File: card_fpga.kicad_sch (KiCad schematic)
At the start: 2 parts, among them U1 LFE5U-25F-6BG381C, Y1 FNETHE025

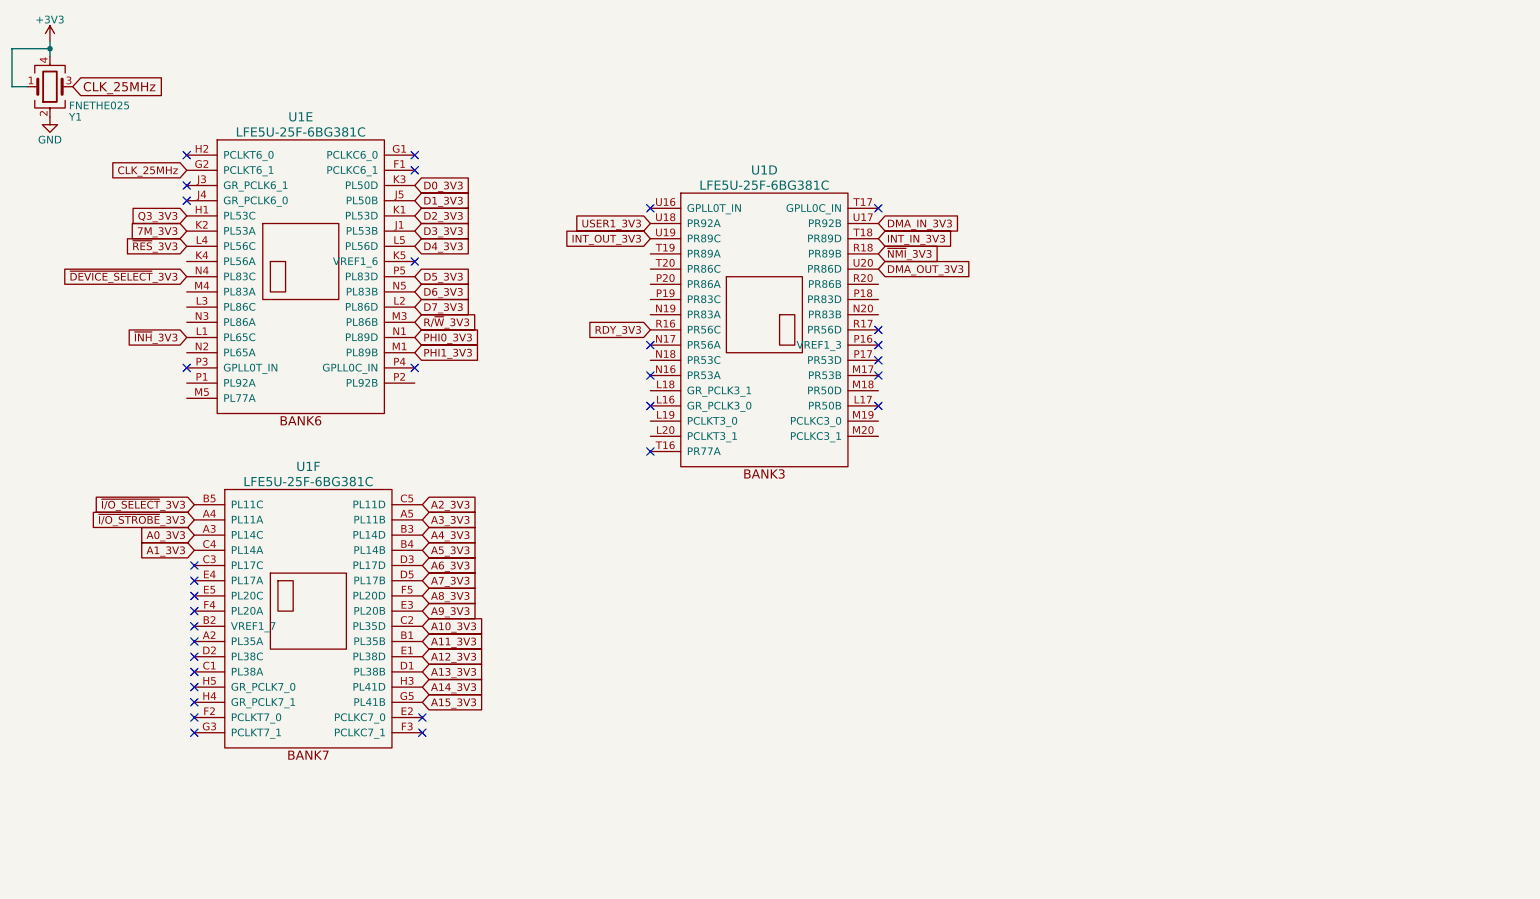
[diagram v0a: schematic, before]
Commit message: Moved routing to right side of FPGA
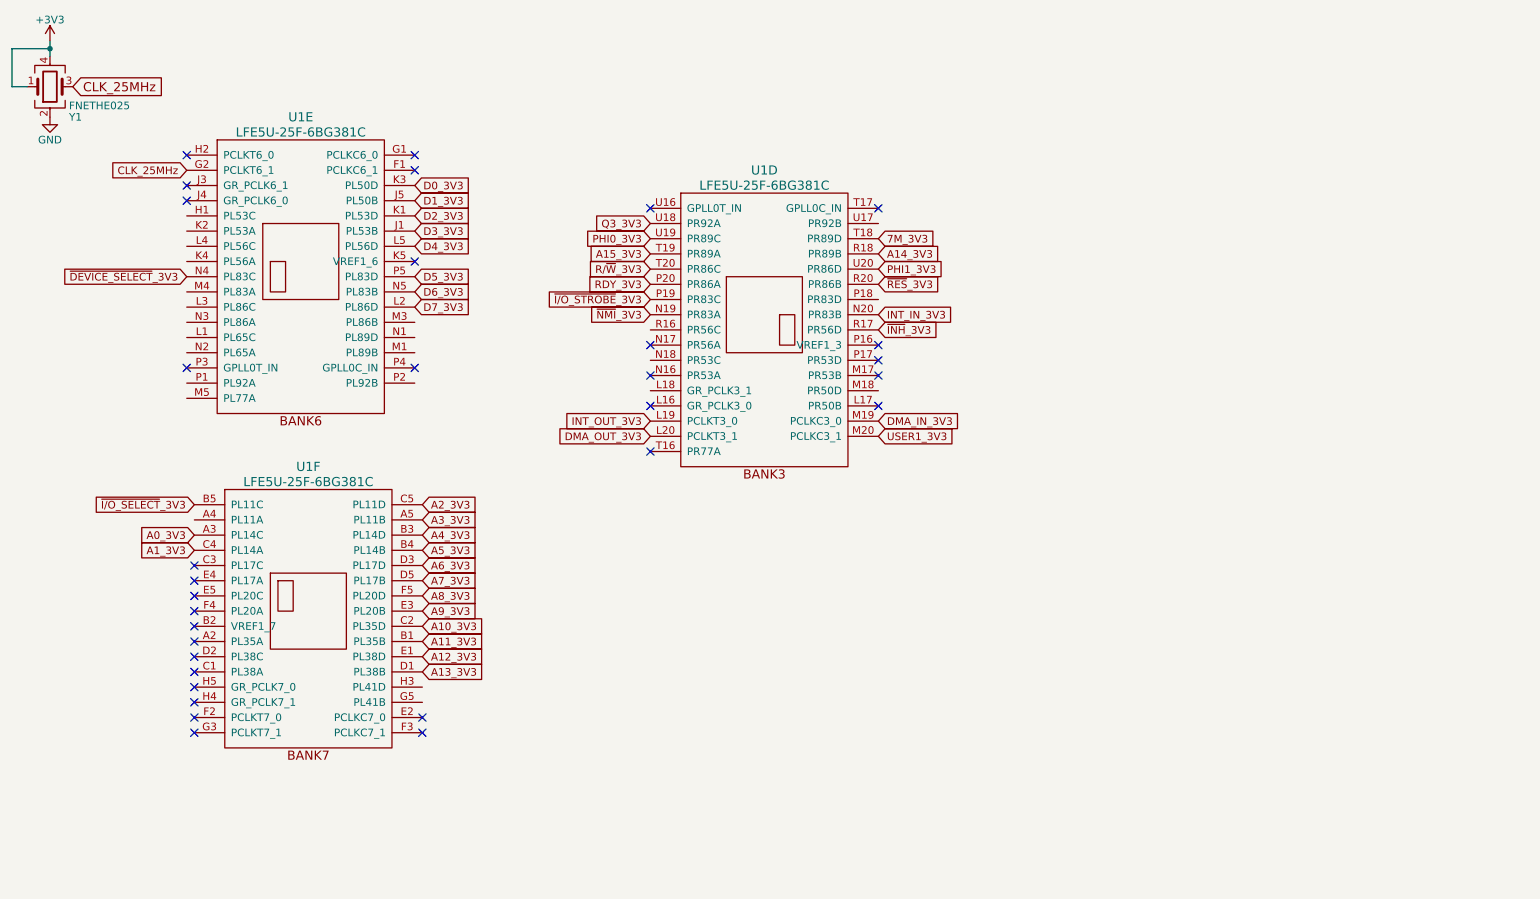
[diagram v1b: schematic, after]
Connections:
- net 7M_3V3: now also U1.T18 (PR89D); no longer U1.K2 (PL53A)
- net A14_3V3: now also U1.R18 (PR89B); no longer U1.H3 (PL41D)
- net A15_3V3: now also U1.T19 (PR89A); no longer U1.G5 (PL41B)
- net DMA_IN_3V3: now also U1.M19 (PCLKC3_0); no longer U1.U17 (PR92B)
- net DMA_OUT_3V3: now also U1.L20 (PCLKT3_1); no longer U1.U20 (PR86D)
- net INT_IN_3V3: now also U1.N20 (PR83B); no longer U1.T18 (PR89D)
- net INT_OUT_3V3: now also U1.L19 (PCLKT3_0); no longer U1.U19 (PR89C)
- net PHI0_3V3: now also U1.U19 (PR89C); no longer U1.N1 (PL89D)
- net PHI1_3V3: now also U1.U20 (PR86D); no longer U1.M1 (PL89B)
- net Q3_3V3: now also U1.U18 (PR92A); no longer U1.H1 (PL53C)
- net RDY_3V3: now also U1.P20 (PR86A); no longer U1.R16 (PR56C)
- net R/~{W}_3V3: now also U1.T20 (PR86C); no longer U1.M3 (PL86B)
- net USER1_3V3: now also U1.M20 (PCLKC3_1); no longer U1.U18 (PR92A)
- net ~{INH}_3V3: now also U1.R17 (PR56D); no longer U1.L1 (PL65C)
- net ~{I/O_STROBE}_3V3: now also U1.P19 (PR83C); no longer U1.A4 (PL11A)
- net ~{NMI}_3V3: now also U1.N19 (PR83A); no longer U1.R18 (PR89B)
- net ~{RES}_3V3: now also U1.R20 (PR86B); no longer U1.L4 (PL56C)
- no-connect marks 33 -> 32

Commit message: Routed Level Shifters + Flash
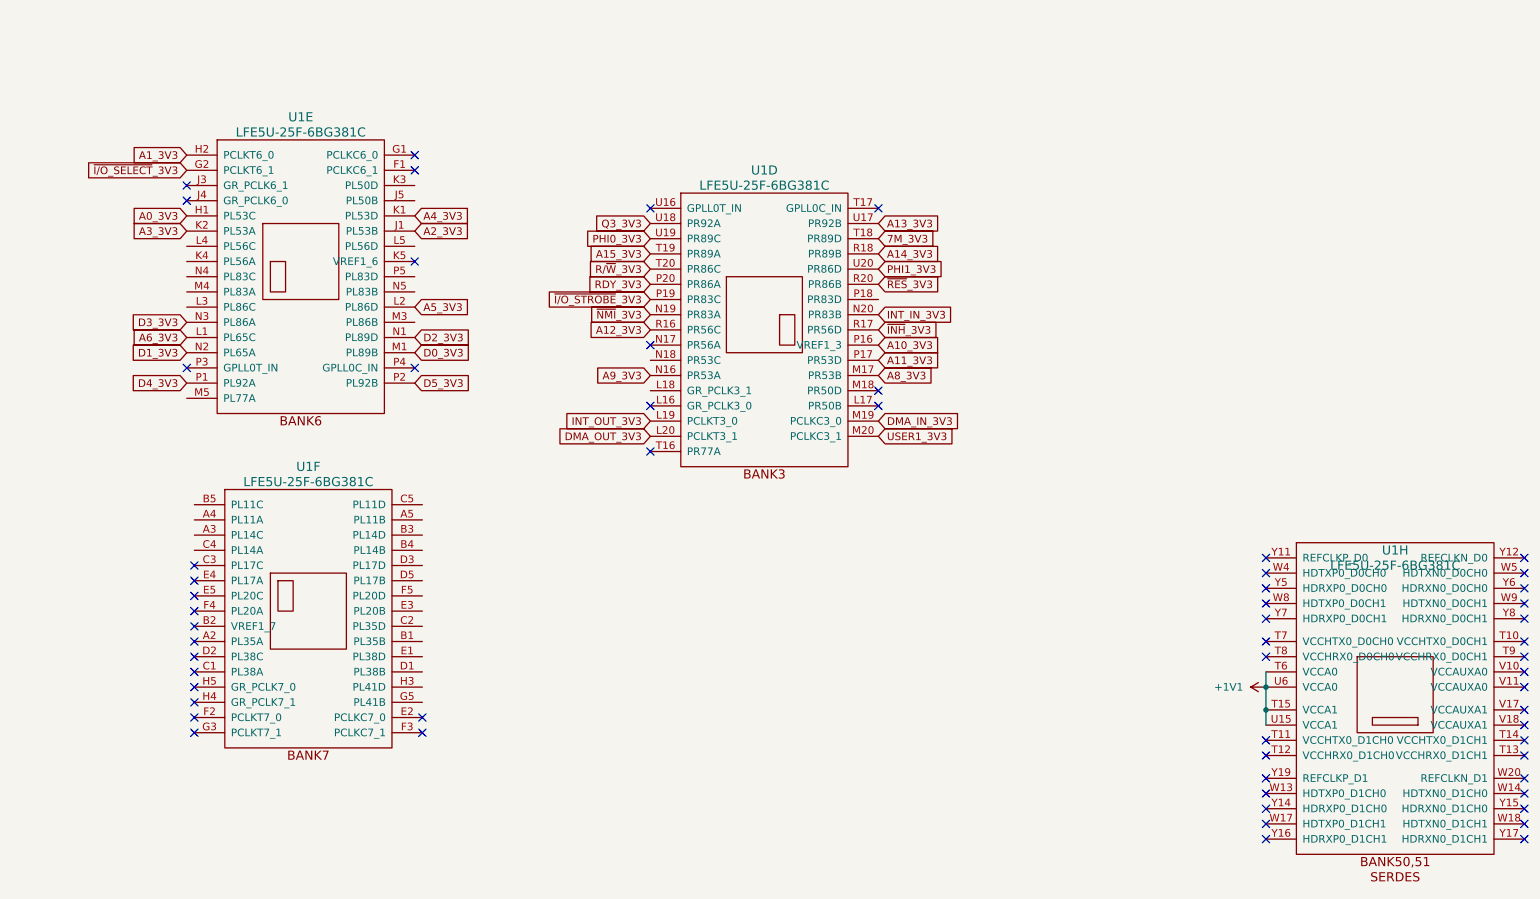
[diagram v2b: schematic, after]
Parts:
- removed Y1: FNETHE025, oscxo:Crystal_SMD_7050_4Pads, symbol Device:Crystal_GND24
- added unit 8 of U1
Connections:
- net CLK_25MHz is gone; now on net ~{I/O_SELECT}_3V3: U1.G2 (PCLKT6_1)
- net D7_3V3 is gone; now on net A5_3V3: U1.L2 (PL86D)
- net A0_3V3: now also U1.H1 (PL53C); no longer U1.A3 (PL14C)
- net A10_3V3: now also U1.P16 (VREF1_3); no longer U1.C2 (PL35D)
- net A11_3V3: now also U1.P17 (PR53D); no longer U1.B1 (PL35B)
- net A12_3V3: now also U1.R16 (PR56C); no longer U1.E1 (PL38D)
- net A13_3V3: now also U1.U17 (PR92B); no longer U1.D1 (PL38B)
- net A1_3V3: now also U1.H2 (PCLKT6_0); no longer U1.C4 (PL14A)
- net A2_3V3: now also U1.J1 (PL53B); no longer U1.C5 (PL11D)
- net A3_3V3: now also U1.K2 (PL53A); no longer U1.A5 (PL11B)
- net A4_3V3: now also U1.K1 (PL53D); no longer U1.B3 (PL14D)
- net A5_3V3: no longer U1.B4 (PL14B)
- net A6_3V3: now also U1.L1 (PL65C); no longer U1.D3 (PL17D)
- net A8_3V3: now also U1.M17 (PR53B); no longer U1.F5 (PL20D)
- net A9_3V3: now also U1.N16 (PR53A); no longer U1.E3 (PL20B)
- net D0_3V3: now also U1.M1 (PL89B); no longer U1.K3 (PL50D)
- net D1_3V3: now also U1.N2 (PL65A); no longer U1.J5 (PL50B)
- net D2_3V3: now also U1.N1 (PL89D); no longer U1.K1 (PL53D)
- net D3_3V3: now also U1.N3 (PL86A); no longer U1.J1 (PL53B)
- net D4_3V3: now also U1.P1 (PL92A); no longer U1.L5 (PL56D)
- net D5_3V3: now also U1.P2 (PL92B); no longer U1.P5 (PL83D)
- net ~{I/O_SELECT}_3V3: no longer U1.B5 (PL11C)
- net A7_3V3: no longer names the net of U1.D5 (PL17B)
- net D6_3V3: no longer names the net of U1.N5 (PL83B)
- net ~{DEVICE_SELECT}_3V3: no longer names the net of U1.N4 (PL83C)
- new net +1V1: U1.T15 (VCCA1), U1.T6 (VCCA0), U1.U15 (VCCA1), U1.U6 (VCCA0)
- no-connect marks 32 -> 60

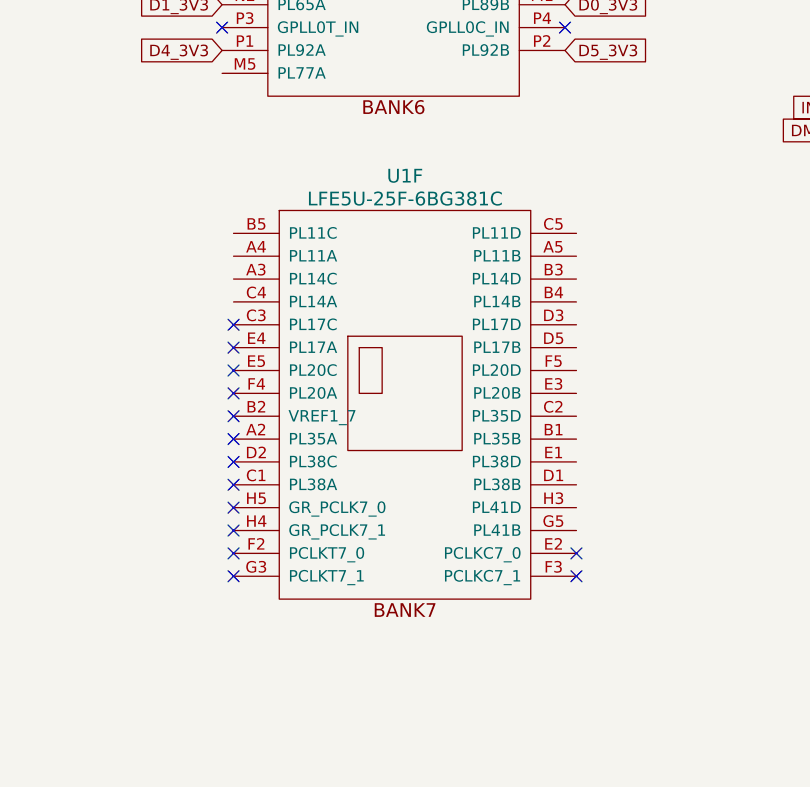
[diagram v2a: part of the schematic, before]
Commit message: Started SRAM routing
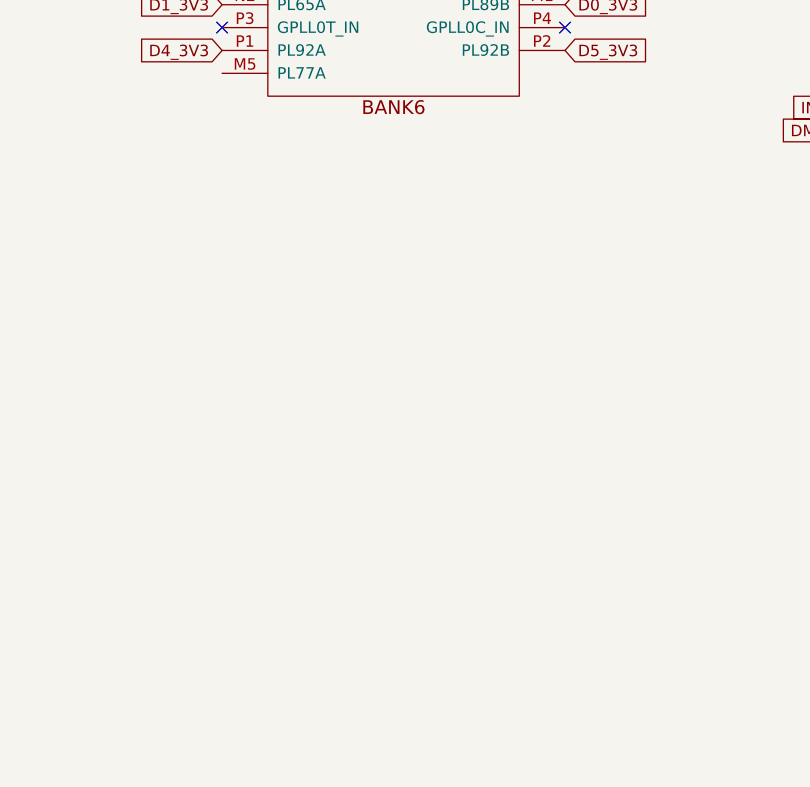
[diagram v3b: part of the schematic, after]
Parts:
- removed unit 6 of U1
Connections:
- no-connect marks 60 -> 46

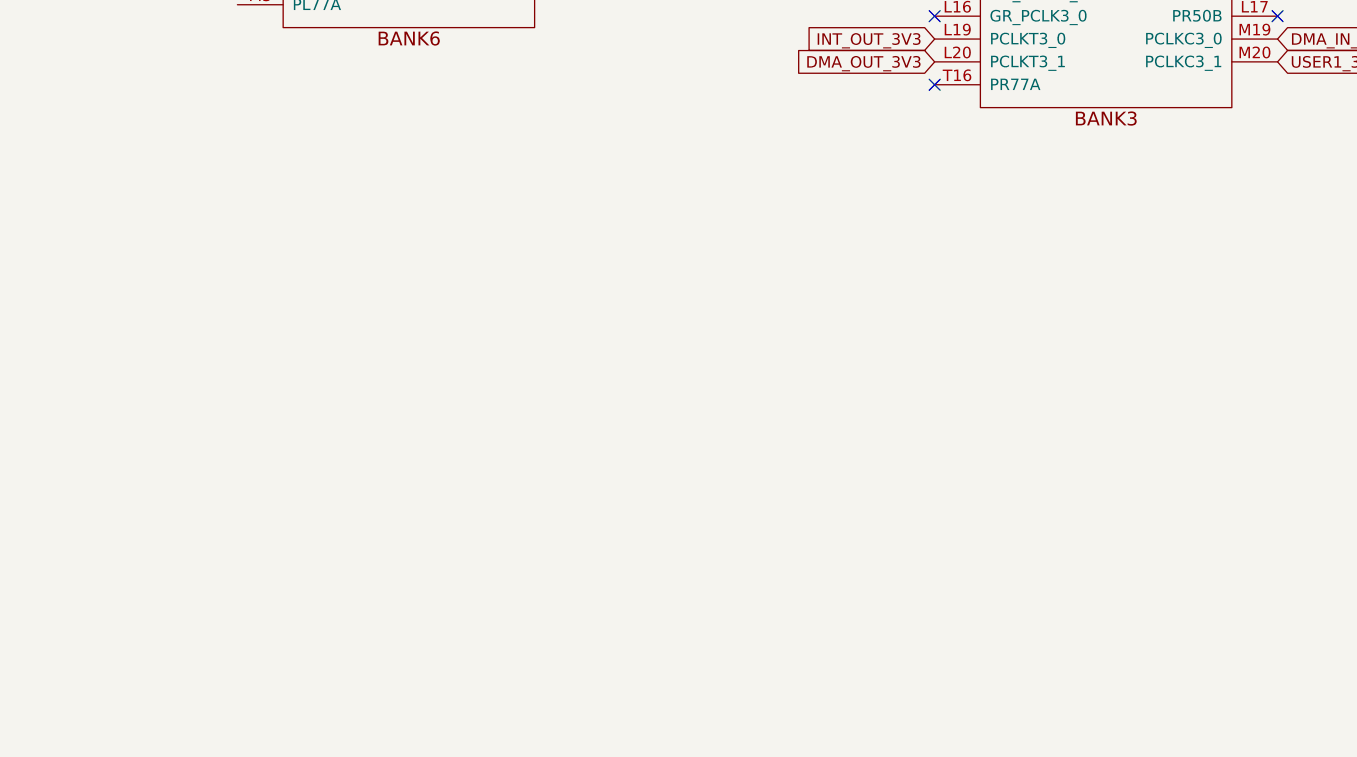
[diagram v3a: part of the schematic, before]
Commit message: Added Breakout pins + logo
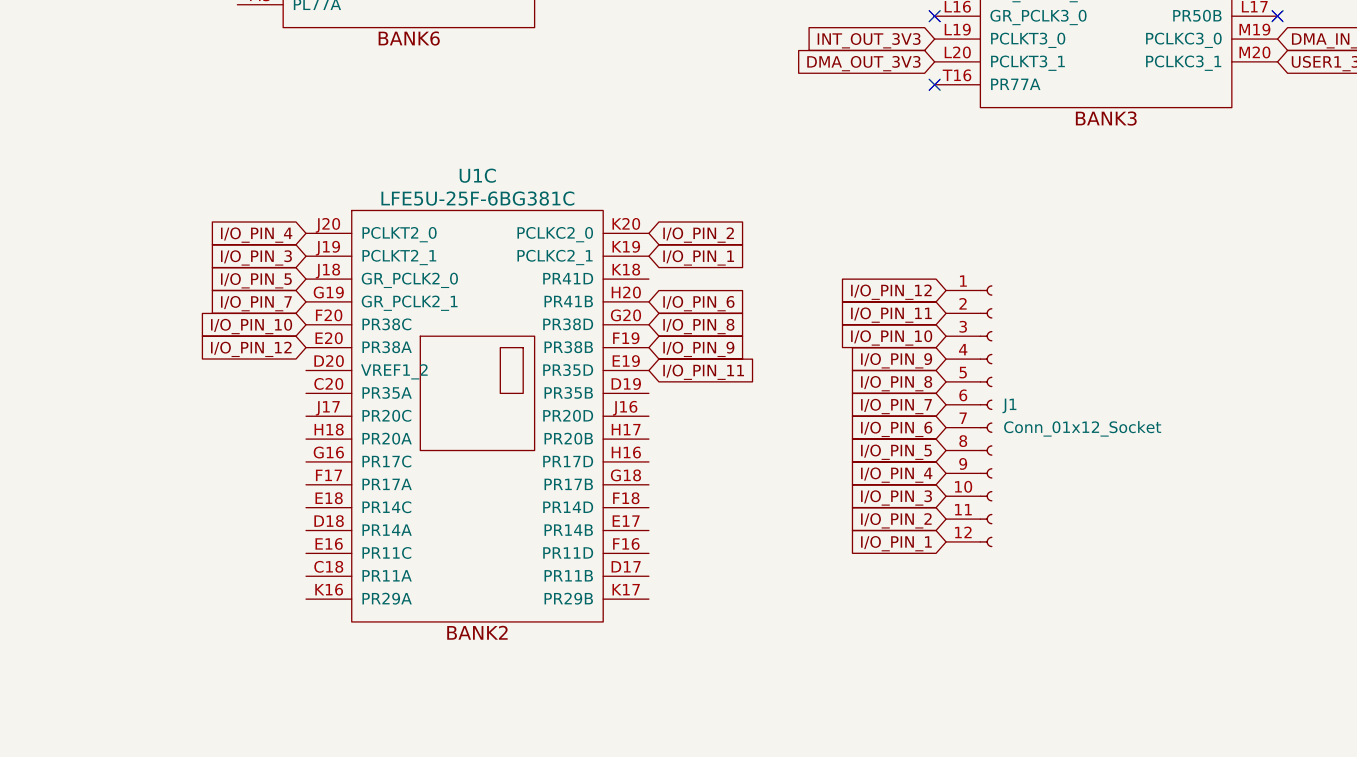
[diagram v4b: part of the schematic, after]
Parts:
- added J1: Conn_01x12_Socket, Connector_PinHeader_2.54mm:PinHeader_1x12_P2.54mm_Horizontal, symbol Connector:Conn_01x12_Socket
- added unit 3 of U1
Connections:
- new net I/O_PIN_1: J1.12 (Pin_12), U1.K19 (PCLKC2_1)
- new net I/O_PIN_10: J1.3 (Pin_3), U1.F20 (PR38C)
- new net I/O_PIN_11: J1.2 (Pin_2), U1.E19 (PR35D)
- new net I/O_PIN_12: J1.1 (Pin_1), U1.E20 (PR38A)
- new net I/O_PIN_2: J1.11 (Pin_11), U1.K20 (PCLKC2_0)
- new net I/O_PIN_3: J1.10 (Pin_10), U1.J19 (PCLKT2_1)
- new net I/O_PIN_4: J1.9 (Pin_9), U1.J20 (PCLKT2_0)
- new net I/O_PIN_5: J1.8 (Pin_8), U1.J18 (GR_PCLK2_0)
- new net I/O_PIN_6: J1.7 (Pin_7), U1.H20 (PR41B)
- new net I/O_PIN_7: J1.6 (Pin_6), U1.G19 (GR_PCLK2_1)
- new net I/O_PIN_8: J1.5 (Pin_5), U1.G20 (PR38D)
- new net I/O_PIN_9: J1.4 (Pin_4), U1.F19 (PR38B)
